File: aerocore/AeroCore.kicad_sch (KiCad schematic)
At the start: 6 parts

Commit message: add firmware and pcb
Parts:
- removed 5V_Power1: Conn_01x02, TerminalBlock:TerminalBlock_Xinya_XY308-2.54-2P_1x02_P2.54mm_Horizontal, symbol Connector_Generic:Conn_01x02
- removed ELRS1, FC1: Conn_01x04, TerminalBlock:TerminalBlock_Xinya_XY308-2.54-4P_1x04_P2.54mm_Horizontal, symbol Connector_Generic:Conn_01x04
- removed RPi_Pico1: Pico, RPi_Pico:RPi_Pico_SMD_TH, symbol RPi_Pico:Pico
- removed RX_SELECT1, TX_SELECT1: SN74LVC2G157DCUR, easyeda2kicad:VSSOP-8_L2.3-W2.0-P0.50-LS3.1-BL, symbol easyeda2kicad:SN74LVC2G157DCUR
- added 5.1k1, 5.1k2: 5.1k, Resistor_SMD:R_0603_1608Metric_Pad0.98x0.95mm_HandSolder, symbol Device:R
- added U1: RP2040, Package_DFN_QFN:QFN-56-1EP_7x7mm_P0.4mm_EP3.2x3.2mm, symbol MCU_RaspberryPi:RP2040
- added USBC1: USB_C_Receptacle_USB2.0_16P, Connector_USB:USB_C_Receptacle_GCT_USB4115-03-C, symbol Connector:USB_C_Receptacle_USB2.0_16P
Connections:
- new net: 5.1k1.1, USBC1.A5 (CC1)
- new net: 5.1k2.1, USBC1.B5 (CC2)
- new net: USBC1.A1 (GND), USBC1.A12 (GND), USBC1.B1 (GND), USBC1.B12 (GND)
- new net: U1.1 (IOVDD), U1.10 (IOVDD), U1.22 (IOVDD), U1.33 (IOVDD), U1.42 (IOVDD), U1.49 (IOVDD)
- new net: U1.23 (DVDD), U1.50 (DVDD)
- new net GND: 5.1k1.2, 5.1k2.2
- new net VBUS: USBC1.A4 (VBUS), USBC1.A9 (VBUS), USBC1.B4 (VBUS), USBC1.B9 (VBUS)

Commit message: make custom rp2040 based design
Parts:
- removed 5.1k1, 5.1k2: 5.1k, Resistor_SMD:R_0603_1608Metric_Pad0.98x0.95mm_HandSolder, symbol Device:R
- removed USBC1: USB_C_Receptacle_USB2.0_16P, Connector_USB:USB_C_Receptacle_GCT_USB4115-03-C, symbol Connector:USB_C_Receptacle_USB2.0_16P
- added BOOT1, RST1: SW_SPST, Button_Switch_SMD:SW_Push_1P1T_NO_CK_KMR2, symbol Switch:SW_SPST
- added C1, C2, C3, C4: 10uF, Capacitor_SMD:C_0805_2012Metric_Pad1.18x1.45mm_HandSolder, symbol Device:C
- added C5, C6: 22pF, Capacitor_SMD:C_0805_2012Metric_Pad1.18x1.45mm_HandSolder, symbol Device:C
- added D1: MBR0540, Diode_SMD:D_SOD-123, symbol Diode:MBR0540
- added D2: NSR0340HT1G, Diode_SMD:D_SOD-323, symbol Diode:NSR0340HT1G
- added D3, D4: RED, LED_SMD:LED_0603_1608Metric_Pad1.05x0.95mm_HandSolder, symbol Device:LED
- added D5: ORANGE, LED_SMD:LED_0603_1608Metric_Pad1.05x0.95mm_HandSolder, symbol Device:LED
- added J1: USB_C_Receptacle_USB2.0_16P, Connector_USB:USB_C_Receptacle_Palconn_UTC16-G, symbol Connector:USB_C_Receptacle_USB2.0_16P
- added J2: Conn_01x03_Pin, Connector_PinHeader_2.54mm:PinHeader_1x03_P2.54mm_Horizontal, symbol Connector:Conn_01x03_Pin
- added J3: Conn_01x02_Pin, Connector_JST:JST_EH_S2B-EH_1x02_P2.50mm_Horizontal, symbol Connector:Conn_01x02_Pin
- added Q1: DMG3418L, Package_TO_SOT_SMD:SOT-23, symbol Transistor_FET:DMG3418L
- added R1, R2: 27, Resistor_SMD:R_0603_1608Metric_Pad0.98x0.95mm_HandSolder, symbol Device:R
- added R10, R11, R5, R6, R7, R8: 10k, Resistor_SMD:R_0603_1608Metric_Pad0.98x0.95mm_HandSolder, symbol Device:R
- added R12, R3, R4: 5.1k, Resistor_SMD:R_0603_1608Metric_Pad0.98x0.95mm_HandSolder, symbol Device:R
- added R13, R9: 1k, Resistor_SMD:R_0603_1608Metric_Pad0.98x0.95mm_HandSolder, symbol Device:R
- added U2: AP2112K-3.3, Package_TO_SOT_SMD:SOT-23-5, symbol Regulator_Linear:AP2112K-3.3
- added U3: MCP73831-2-OT, Package_TO_SOT_SMD:SOT-23-5, symbol Battery_Management:MCP73831-2-OT
- added Y2: 12MHz, Crystal:Crystal_SMD_2520-4Pin_2.5x2.0mm, symbol Device:Crystal_GND24
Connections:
- net GND: now also U1.19 (TESTEN), U1.57 (GND), BOOT1.2 (B), C1.2, C2.2, C3.2, C4.2, C5.1, C6.1, D3.1 (K), D4.1 (K), J1.A1 (GND), J1.A12 (GND), J1.B1 (GND), J1.B12 (GND), J2.2 (Pin_2), J3.2 (Pin_2), R12.2, R3.2, R4.1, R5.2, RST1.2 (B), U2.2 (GND), U3.2 (V_{SS}), Y2.2, Y2.4
- net VBUS: now also D1.2 (A), D5.2 (A), J1.A4 (VBUS), J1.A9 (VBUS), J1.B4 (VBUS), J1.B9 (VBUS), Q1.1 (G), R5.1, U3.4 (V_{DD})
- net D13: now reaches U1.16 (GPIO13)
- net D13: now also R10.1
- net D14: now reaches U1.17 (GPIO14)
- net D14: now also R8.1
- net XIN: now reaches U1.20 (XIN)
- net XIN: now also C5.2, Y2.1
- net XOUT: now reaches U1.21 (XOUT)
- net XOUT: now also R13.2
- net SWCLK: now reaches U1.24 (SWCLK)
- net SWCLK: now also J2.3 (Pin_3)
- net SWDIO: now reaches U1.25 (SWD)
- net SWDIO: now also J2.1 (Pin_1)
- net ~{RESET}: now reaches U1.26 (RUN)
- net ~{RESET}: now also R7.2, RST1.1 (A)
- net D-: now reaches U1.46 (USB_DM)
- net D-: now also R1.2
- net D+: now reaches U1.47 (USB_DP)
- net D+: now also R2.2
- net QSPI_CS: now reaches U1.56 (QSPI_SS)
- net QSPI_CS: now also R9.1
- new net: D3.2 (A), R10.2
- new net: C3.1, D1.1 (K), Q1.2 (S), R6.1, U2.1 (VIN)
- new net: BOOT1.1 (A), D2.1 (K)
- new net: J1.A7 (D-), J1.B7 (D-), R1.1
- new net: C6.2, R13.1, Y2.3
- new net: J1.A6 (D+), J1.B6 (D+), R2.1
- new net: R6.2, U2.3 (EN)
- new net: D2.2 (A), R9.2
- new net: D4.2 (A), R8.2
- new net: J1.A5 (CC1), R3.1
- new net: J1.B5 (CC2), R4.2
- new net: D5.1 (K), R11.2
- new net: R11.1, U3.1 (STAT)
- new net: R12.1, U3.5 (PROG)
- new net +3v3: C1.1, C2.1, R7.1, U2.5 (VOUT)
- new net VBAT: C4.1, J3.1 (Pin_1), Q1.3 (D), U3.3 (V_{BAT})

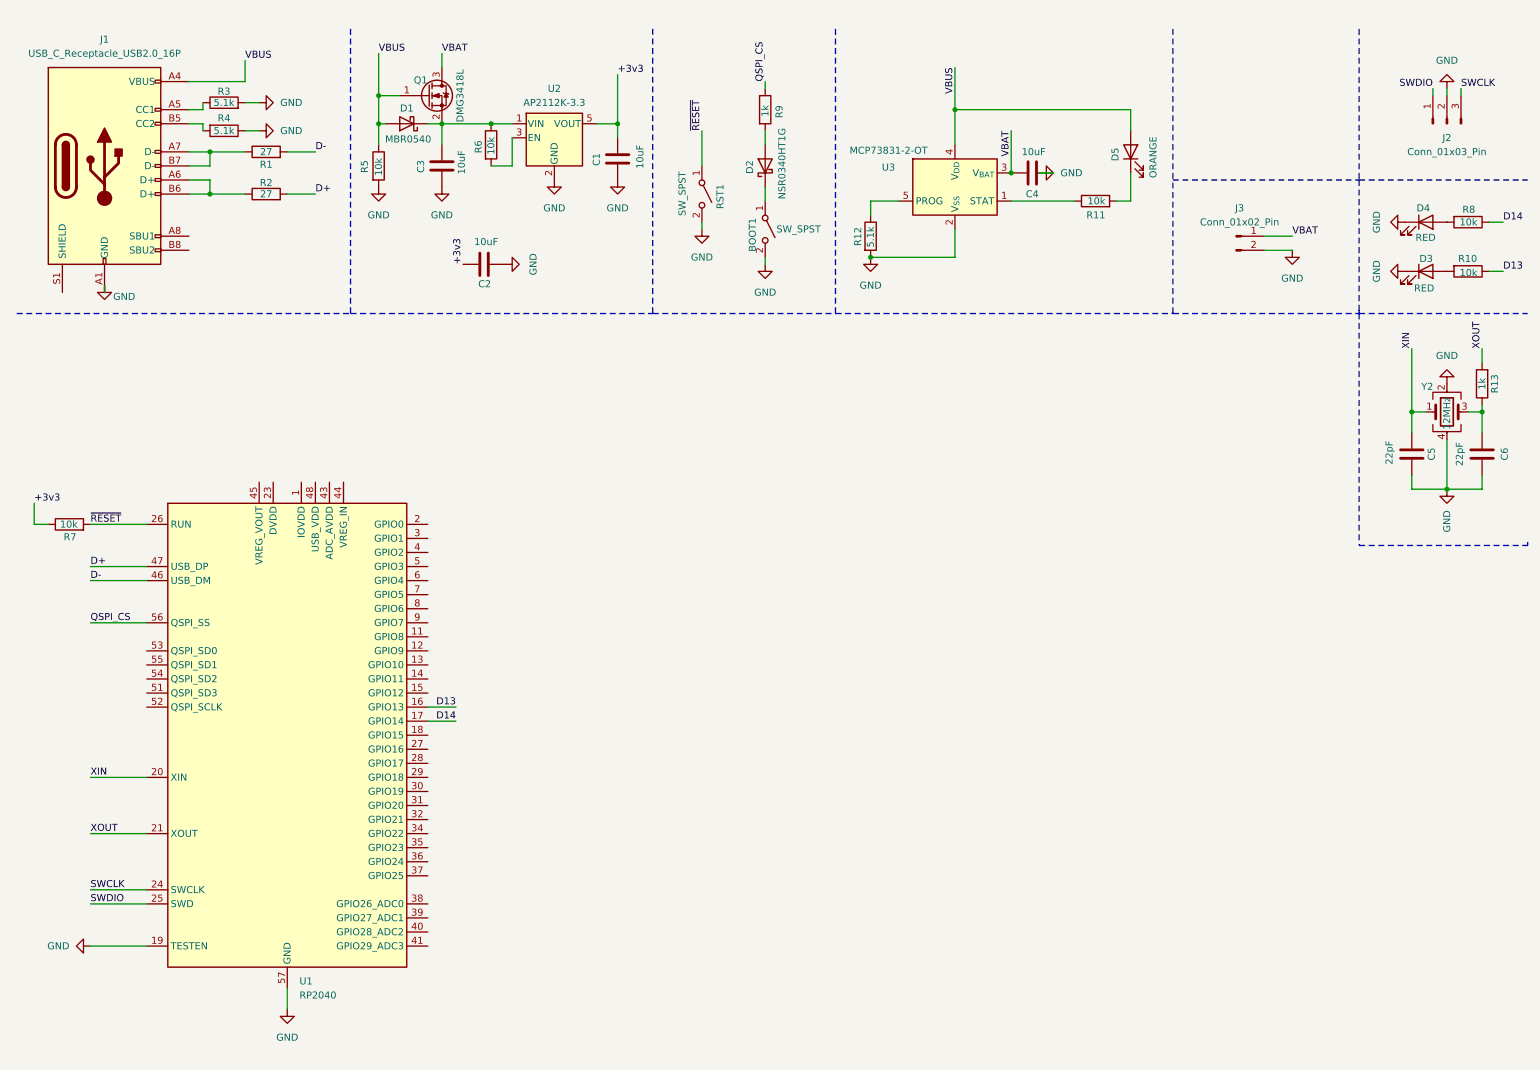
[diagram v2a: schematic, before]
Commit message: add sensors to schematics
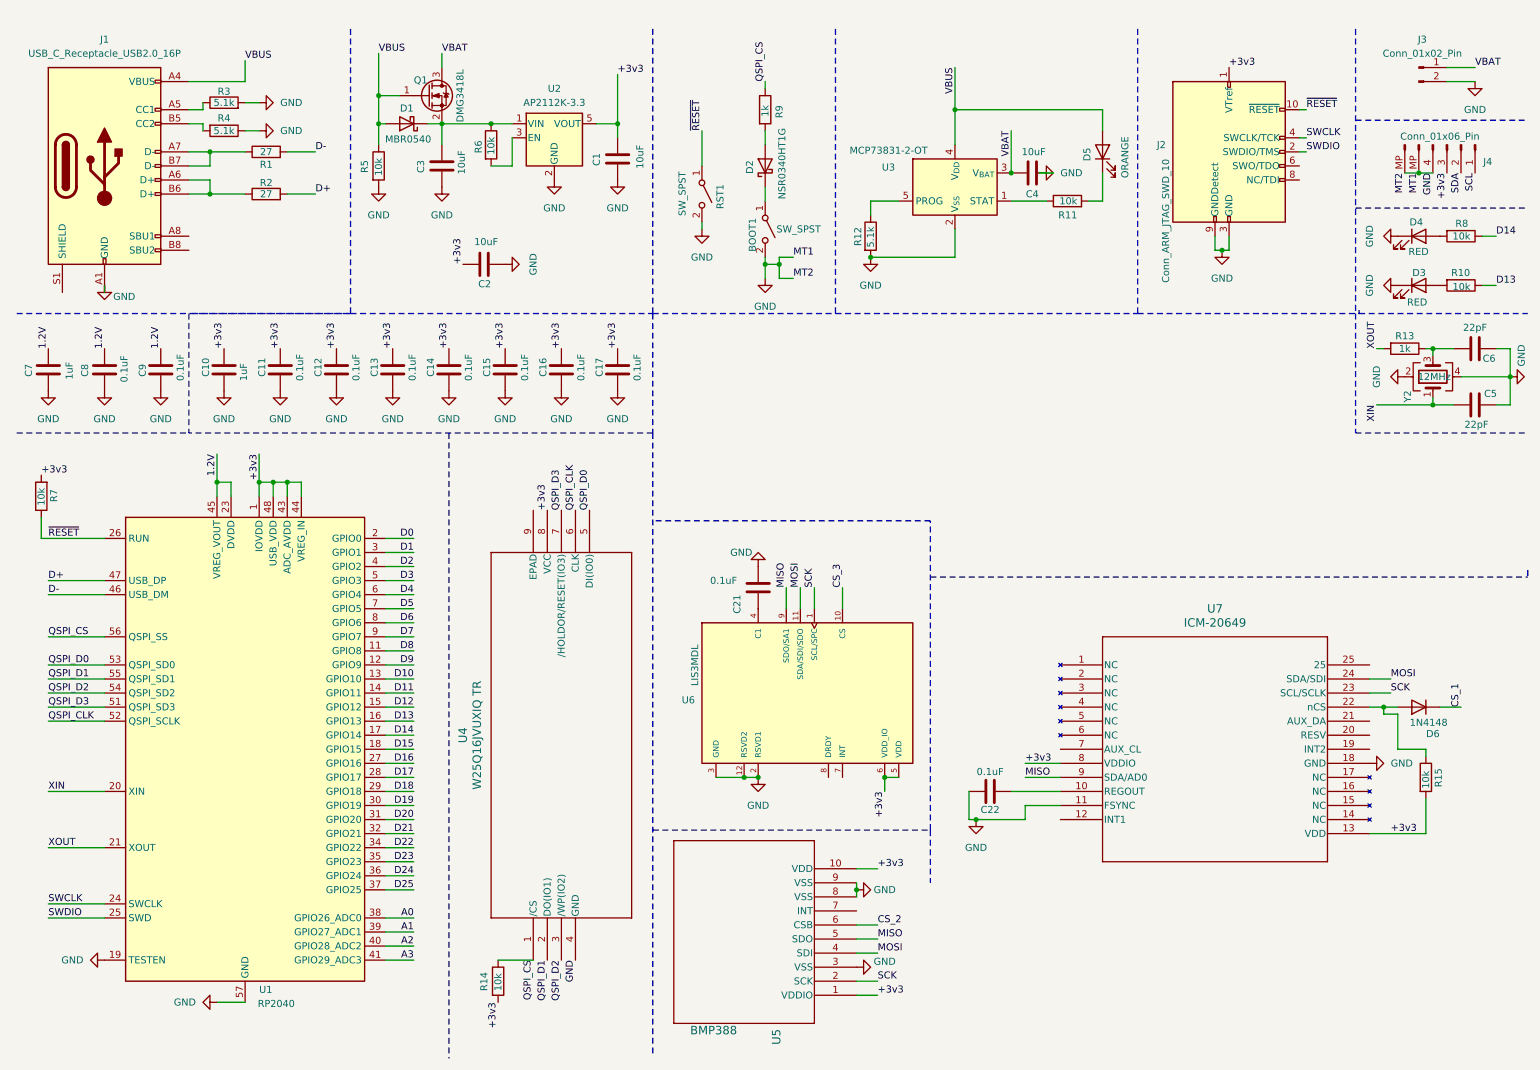
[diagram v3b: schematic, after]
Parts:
- removed J2: Conn_01x03_Pin, Connector_PinHeader_2.54mm:PinHeader_1x03_P2.54mm_Horizontal, symbol Connector:Conn_01x03_Pin
- added C10, C7: 1uF, Capacitor_SMD:C_0603_1608Metric_Pad1.08x0.95mm_HandSolder, symbol Device:C
- added C11, C12, C13, C14, C15, C16, C17, C8, C9: 0.1uF, Capacitor_SMD:C_0603_1608Metric_Pad1.08x0.95mm_HandSolder, symbol Device:C
- added C21, C22: 0.1uF, symbol Device:C
- added D6: 1N4148, Diode_THT:D_DO-35_SOD27_P7.62mm_Horizontal, symbol Diode:1N4148
- added J2: Conn_ARM_JTAG_SWD_10, Connector_PinSocket_1.27mm:PinSocket_2x05_P1.27mm_Vertical_SMD, symbol Connector:Conn_ARM_JTAG_SWD_10
- added J4: Conn_01x06_Pin, Connector_JST:JST_SH_SM04B-SRSS-TB_1x04-1MP_P1.00mm_Horizontal, symbol Connector:Conn_01x06_Pin
- added R14: 10k, Resistor_SMD:R_0603_1608Metric_Pad0.98x0.95mm_HandSolder, symbol Device:R
- added R15: 10k, symbol Device:R
- added U4: W25Q16JVUXIQ TR, Package_SON:Winbond_USON-8-1EP_3x2mm_P0.5mm_EP0.2x1.6mm, symbol 2024-07-29_14-51-39:W25Q16JVUXIQ_TR
- added U5: BMP388, Package_LGA:Bosch_LGA-8_2x2.5mm_P0.65mm_ClockwisePinNumbering, symbol 2024-07-29_16-49-53:BMP388
- added U6: LIS3MDL, LIS3MDL:XDCR_LIS3MDL, symbol LIS3MDL:LIS3MDL
- added U7: ICM-20649, QFN24_3X3X0P9_IVS, symbol 2024-07-29_16-51-12:ICM-20649
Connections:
- net +3v3: now also R7.2, U1.1 (IOVDD), U1.10 (IOVDD), U1.22 (IOVDD), U1.33 (IOVDD), U1.42 (IOVDD), U1.43 (ADC_AVDD), U1.44 (VREG_IN), U1.48 (USB_VDD), U1.49 (IOVDD), C10.1, C11.1, C12.1, C13.1, C14.1, C15.1, C16.1, C17.1, J2.1 (VTref), J4.3 (Pin_3), R14.2, R15.2, U4.8 (VCC), U5.1 (VDDIO), U5.10 (VDD), U6.5 (VDD), U6.6 (VDD_IO), U7.13 (VDD), U7.8 (VDDIO); no longer R7.1
- net GND: now also C10.2, C11.2, C12.2, C13.2, C14.2, C15.2, C16.2, C17.2, C21.2, C22.1, C7.2, C8.2, C9.2, J2.3 (GND), J2.5 (GND), J2.9 (GNDDetect), J4.4 (Pin_4), J4.MP (Pin_6), U4.4 (GND), U5.3 (VSS), U5.8 (VSS), U5.9 (VSS), U6.12 (RSVD2), U6.2 (RSVD1), U6.3 (GND), U7.11 (FSYNC), U7.18 (GND)
- net QSPI_CS: now also R14.1, U4.1 (/CS)
- net SWCLK: now also J2.4 (SWCLK/TCK)
- net SWDIO: now also J2.2 (SWDIO/TMS)
- net ~{RESET}: now also R7.1, J2.10 (~{RESET}); no longer R7.2
- net D8: now reaches U1.11 (GPIO8)
- net D9: now reaches U1.12 (GPIO9)
- net D10: now reaches U1.13 (GPIO10)
- net D11: now reaches U1.14 (GPIO11)
- net D12: now reaches U1.15 (GPIO12)
- net D15: now reaches U1.18 (GPIO15)
- net D0: now reaches U1.2 (GPIO0)
- net 1.2V: now reaches U1.23 (DVDD), U1.50 (DVDD)
- net 1.2V: now also U1.45 (VREG_VOUT), C7.1, C8.1, C9.1
- net D16: now reaches U1.27 (GPIO16)
- net D17: now reaches U1.28 (GPIO17)
- net D18: now reaches U1.29 (GPIO18)
- net D1: now reaches U1.3 (GPIO1)
- net D19: now reaches U1.30 (GPIO19)
- net D20: now reaches U1.31 (GPIO20)
- net D21: now reaches U1.32 (GPIO21)
- net D22: now reaches U1.34 (GPIO22)
- net D23: now reaches U1.35 (GPIO23)
- net D24: now reaches U1.36 (GPIO24)
- net D25: now reaches U1.37 (GPIO25)
- net A0: now reaches U1.38 (GPIO26_ADC0)
- net A1: now reaches U1.39 (GPIO27_ADC1)
- net D2: now reaches U1.4 (GPIO2)
- net A2: now reaches U1.40 (GPIO28_ADC2)
- net A3: now reaches U1.41 (GPIO29_ADC3)
- net D3: now reaches U1.5 (GPIO3)
- net QSPI_D3: now reaches U1.51 (QSPI_SD3)
- net QSPI_D3: now also U4.7 (/HOLDOR/RESET(IO3))
- net QSPI_CLK: now reaches U1.52 (QSPI_SCLK)
- net QSPI_CLK: now also U4.6 (CLK)
- net QSPI_D0: now reaches U1.53 (QSPI_SD0)
- net QSPI_D0: now also U4.5 (DI(IO0))
- net QSPI_D2: now reaches U1.54 (QSPI_SD2)
- net QSPI_D2: now also U4.3 (/WP(IO2))
- net QSPI_D1: now reaches U1.55 (QSPI_SD1)
- net QSPI_D1: now also U4.2 (DO(IO1))
- net D4: now reaches U1.6 (GPIO4)
- net D5: now reaches U1.7 (GPIO5)
- net D6: now reaches U1.8 (GPIO6)
- net D7: now reaches U1.9 (GPIO7)
- new net: C22.2, U7.10 (REGOUT)
- new net: D6.2 (A), R15.1, U7.22 (nCS)
- new net: C21.1, U6.4 (C1)
- new net CS_1: D6.1 (K)
- new net CS_2: U5.6 (CSB)
- new net CS_3: U6.10 (CS)
- new net MISO: U5.5 (SDO), U6.9 (SDO/SA1), U7.9 (SDA/AD0)
- new net MOSI: U5.4 (SDI), U6.11 (SDA/SDI/SDO), U7.24 (SDA/SDI)
- new net SCK: U5.2 (SCK), U6.1 (SCL/SPC), U7.23 (SCL/SCLK)
- new net SCL: J4.1 (Pin_1)
- new net SDA: J4.2 (Pin_2)
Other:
- moved on the sheet: C5, C6, D3, D4, D5, J3, R10, R11, R13, R7, R8, U1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

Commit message: update info for lis3mdltr
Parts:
- C21, C22: footprint (none) -> Capacitor_SMD:C_0603_1608Metric_Pad1.08x0.95mm_HandSolder
- R15: footprint (none) -> Resistor_SMD:R_0603_1608Metric_Pad0.98x0.95mm_HandSolder
- U6: footprint LIS3MDL:XDCR_LIS3MDL -> Connector_PinHeader_1.00mm:PinHeader_2x06_P1.00mm_Vertical
- U7: footprint QFN24_3X3X0P9_IVS -> Connector_PinHeader_1.00mm:PinHeader_2x09_P1.00mm_Vertical
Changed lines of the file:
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@@
 			)
 		)
-		(property "Footprint" "QFN24_3X3X0P9_IVS"
+		(property "Footprint" "Connector_PinHeader_1.00mm:PinHeader_2x09_P1.00mm_Vertical"
 			(at 200.66 127 0)
 			(effects
@@
 			)
 		)
-		(property "Footprint" "LIS3MDL:XDCR_LIS3MDL"
+		(property "Footprint" "Connector_PinHeader_1.00mm:PinHeader_2x06_P1.00mm_Vertical"
 			(at 156.21 132.08 0)
 			(effects
@@
 			)
 		)
-		(property "Footprint" ""
+		(property "Footprint" "Capacitor_SMD:C_0603_1608Metric_Pad1.08x0.95mm_HandSolder"
 			(at 145.0848 109.22 0)
 			(effects
@@
 			)
 		)
-		(property "Footprint" ""
+		(property "Footprint" "Resistor_SMD:R_0603_1608Metric_Pad0.98x0.95mm_HandSolder"
 			(at 264.922 147.32 90)
 			(effects
@@
 			)
 		)
-		(property "Footprint" ""
+		(property "Footprint" "Capacitor_SMD:C_0603_1608Metric_Pad1.08x0.95mm_HandSolder"
 			(at 191.77 148.8948 0)
 			(effects

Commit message: add files for final board
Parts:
- added D7, D8: RED, LED_SMD:LED_0603_1608Metric_Pad1.05x0.95mm_HandSolder, symbol Device:LED
- added R16, R17: 10k, Resistor_SMD:R_0603_1608Metric_Pad0.98x0.95mm_HandSolder, symbol Device:R
- U5: footprint Package_LGA:Bosch_LGA-8_2x2.5mm_P0.65mm_ClockwisePinNumbering -> easyeda2kicad:SENSORM-SMD_BMP388
- U6: footprint Connector_PinHeader_1.00mm:PinHeader_2x06_P1.00mm_Vertical -> easyeda2kicad:LGA-12_L2.0-W2.0-P0.50-BL
- U7: footprint Connector_PinHeader_1.00mm:PinHeader_2x09_P1.00mm_Vertical -> easyeda2kicad:QFN-24_L3.0-W3.0-P0.40-TL-EP1.4
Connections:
- net D1 is gone; now on net CS_2: U1.3 (GPIO1)
- net D17 is gone; now on net CS_3: U1.28 (GPIO17)
- net D5 is gone; now on net CS_1: U1.7 (GPIO5)
- net D6 is gone; now on net SDA: U1.8 (GPIO6)
- net D7 is gone; now on net SCL: U1.9 (GPIO7)
- net MISO is gone; now on net MISO0: U5.5 (SDO), U6.9 (SDO/SA1), U7.9 (SDA/AD0)
- net MOSI is gone; now on net MOSI0: U5.4 (SDI), U6.11 (SDA/SDI/SDO), U7.24 (SDA/SDI)
- net SCK is gone; now on net SCK0: U5.2 (SCK), U6.1 (SCL/SPC), U7.23 (SCL/SCLK)
- net D13: now also R17.1; no longer R10.1
- net D14: now also R16.1; no longer R8.1
- net D15: now also R10.1
- net D16: now also R8.1
- net GND: now also D7.1 (K), D8.1 (K)
- net D2 renamed SCK0
- net D3 renamed MOSI0
- net D4 renamed MISO0
- new net: D8.2 (A), R17.2
- new net: D7.2 (A), R16.2
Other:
- moved on the sheet: C5, C6, R13, Y2
